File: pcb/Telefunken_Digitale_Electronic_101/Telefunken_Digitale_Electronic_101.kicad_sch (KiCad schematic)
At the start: 0 parts

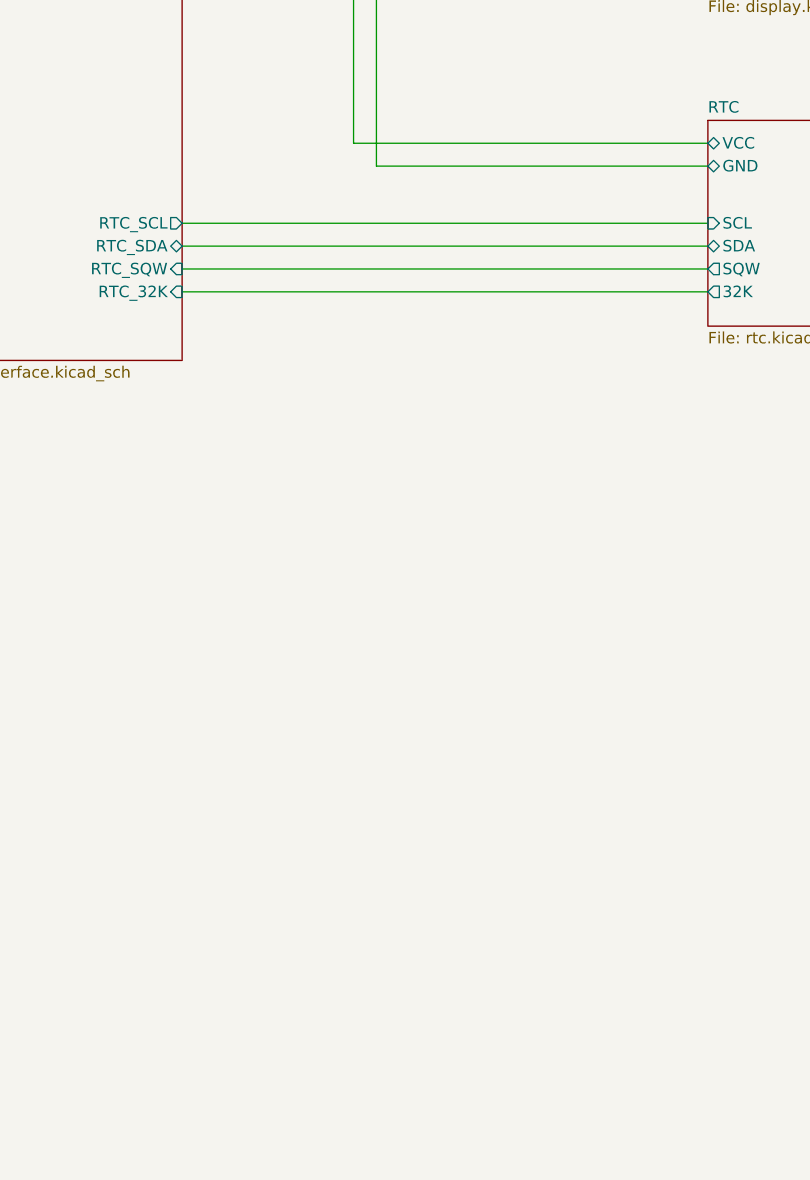
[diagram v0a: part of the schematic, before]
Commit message: PCBs: updated logo; added I2C resistors to I2C (core pcb)
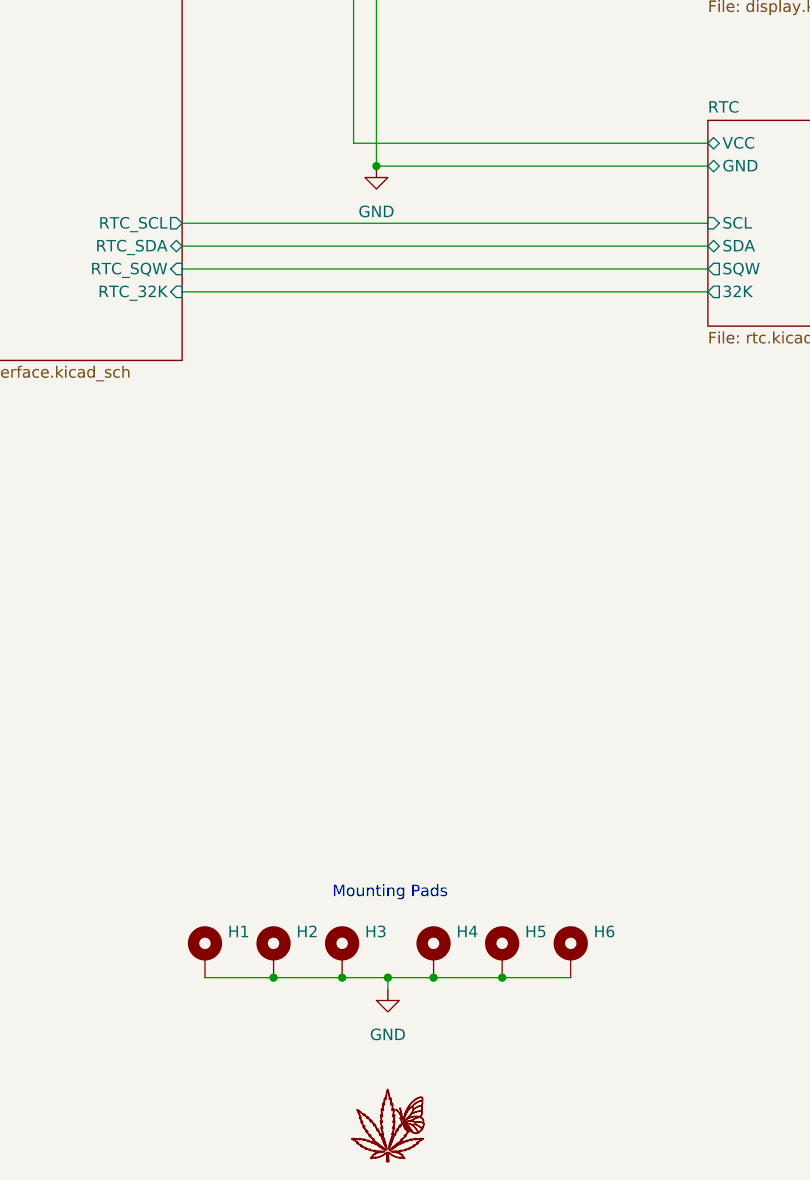
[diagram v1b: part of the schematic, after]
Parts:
- added G1: LOGO, RadioWecker:LOGO, symbol RadioWecker:LOGO
- added H1, H2, H3, H4, H5, H6: MountingHole_Pad_MP, RadioWecker:BOARD_TO_BOARD_PAD_SMD, symbol Mechanical:MountingHole_Pad_MP
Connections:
- new net GND: H1.MP, H2.MP, H3.MP, H4.MP, H5.MP, H6.MP
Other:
- note added: "Mounting Pads"
